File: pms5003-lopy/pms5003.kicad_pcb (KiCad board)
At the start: 2 copper layers, 60 x 56 mm, 24 parts, among them J1 Battery, J2 DS3231, J3 PMS5003, J4 SHT10, J5 P2, J6 PROG, J7 USB_OTG, Q1 IRF540N, Q2 IRF7309IPBF, U1 U3V12F5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

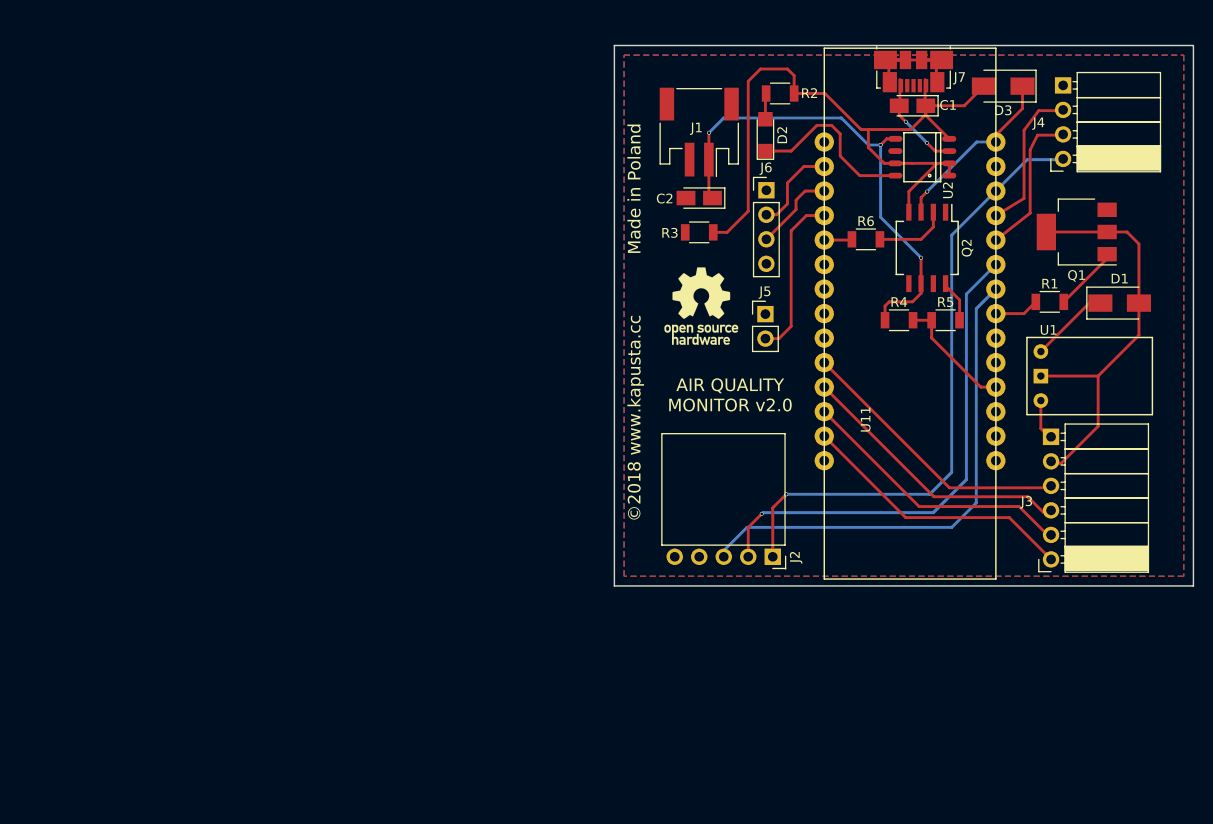
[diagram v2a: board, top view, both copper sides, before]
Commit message: PMS5003-lopy with AQ monitor on the board
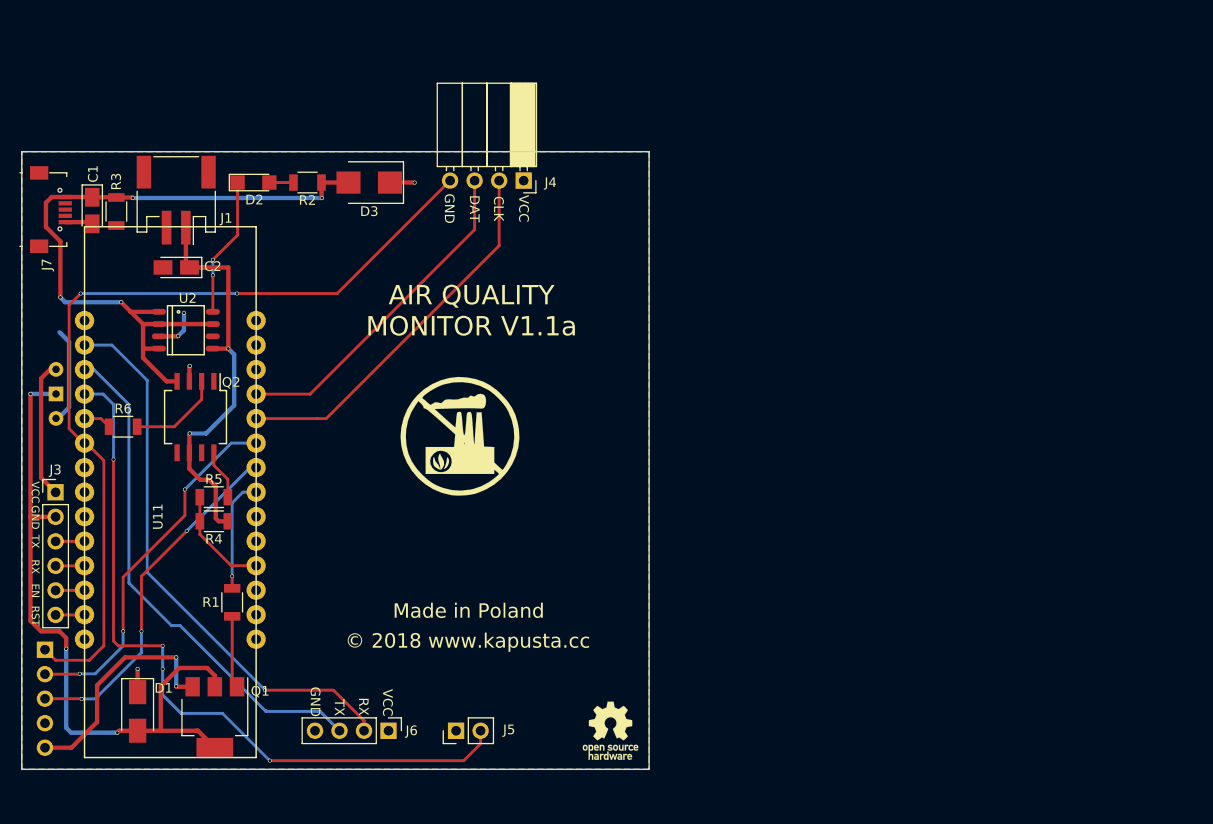
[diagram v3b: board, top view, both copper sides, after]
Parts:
- removed the REF*** at (130.0, 52.0)
- added G***: LOGO, various:pollution, F.Cu at (105.0, 65.5)
- added REF***: OSHW-Logo_5.7x6mm_SilkScreen, Symbols:OSHW-Logo_5.7x6mm_SilkScreen, F.Cu at (120.6, 96.0)
- D3: footprint Diodes_SMD:D_SMA -> Diodes_SMD:D_SMB
- J2, U1: moved to B.Cu
- J3: footprint PMS5003 -> Pin_Headers:Pin_Header_Straight_1x06_Pitch2.54mm
- J4: footprint SHT10 -> Socket_Strips:Socket_Strip_Angled_1x04_Pitch2.54mm
- J7: footprint Connectors_USB:USB_Micro-B_Molex_47346-0001 -> various:USB_Micro-B_91-US01-517
- R2: value 100 -> 470
- moved D1 110.2 mm to (71.6, 94.0), turned to 270 degrees
- moved J3 103.4 mm to (63.1, 71.3), turned to 0 degrees
- moved U1 102.5 mm to (74.7, 65.1)
- moved Q1 102.5 mm to (79.6, 94.6), turned to 270 degrees
- moved J7 90.7 mm to (62.6, 42.0), turned to 270 degrees
- moved R1 90.3 mm to (81.4, 82.7), turned to 270 degrees
- moved C1 85.7 mm to (66.9, 42.1), turned to 270 degrees
- moved R6 79.4 mm to (70.1, 64.5)
- moved U11 78.9 mm to (66.1, 53.5)
- moved U2 78.4 mm to (76.6, 54.5), turned to 270 degrees
- moved R5 78.0 mm to (79.5, 71.8)
- moved Q2 77.8 mm to (77.6, 63.5)
- moved J2 76.0 mm to (62.0, 87.6), turned to 180 degrees
- moved R4 74.0 mm to (79.5, 74.3), turned to 180 degrees
- moved J6 68.3 mm to (97.6, 96.0), turned to 270 degrees
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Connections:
- J2 pad 1: 3V3 -> SHT_RTC_VCC
- J4 pad 4: 3V3 -> SHT_RTC_VCC
- U11 pad 24: SHT10_DATA -> SHT10_SCK
- U11 pad 25: SHT10_SCK -> SHT10_DATA
- U11 pad 26: 3V3 -> (no net)
- U11 pad 6: (no net) -> SHT_RTC_VCC
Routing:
- net SHT_RTC_VCC: track 0.00 -> 89.1 mm, vias 0 -> 2
- net 3V3: track 64.5 -> 0.00 mm, vias 1 -> 0
- net P2: track 17.2 -> 76.2 mm, vias 0 -> 4
- net RX: track 9.34 -> 57.8 mm, vias 0 -> 1
- net TX: track 8.65 -> 53.0 mm
- net 5V_GND: track 43.2 -> 72.1 mm, vias 0 -> 3
- net Net-(J3-Pad6): track 29.0 -> 3.01 mm
- net Net-(J3-Pad4): track 28.9 -> 3.01 mm
- net Net-(J3-Pad5): track 28.9 -> 3.01 mm
- net Net-(J3-Pad3): track 28.9 -> 3.01 mm
- net SHT10_SCK: track 15.3 -> 39.3 mm
- net -USB: track 11.0 -> 32.0 mm, vias 2 -> 4
- net SHT10_DATA: track 15.5 -> 34.8 mm
- net RTC_SCL: track 51.8 -> 36.4 mm, vias 0 -> 3
- net Net-(J7-Pad6): track 14.9 -> 0.00 mm
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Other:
- board size 60 x 56 mm -> 65 x 64 mm
- net class Power added: clearance 0.2, trace_width 0.45, via_dia 0.4, via_drill 0.3
- board text added: "AIR QUALITY MONITOR V1.1a"
- board text added: "CLK"
- board text added: "DAT"
- board text added: "EN"
- board text added: "GND"
- board text added: "Made in Poland"
- board text added: "RST"
- board text added: "RX"
- board text added: "SCL"
- board text added: "SDA"
- board text added: "TX"
- board text added: "VCC"
- board text added: "VIN"
- board text added: "VOUT"
- board text added: "© 2018 www.kapusta.cc"
- board text removed: "AIR QUALITY MONITOR v2.0"
- board text removed: "Prasłowiańska grusza chroni w swych konarach plebejskiego uciekiniera"
- board text removed: "©2018 www.kapusta.cc Made in Poland"

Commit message: Add a pull-up resistor to RTC_VCC
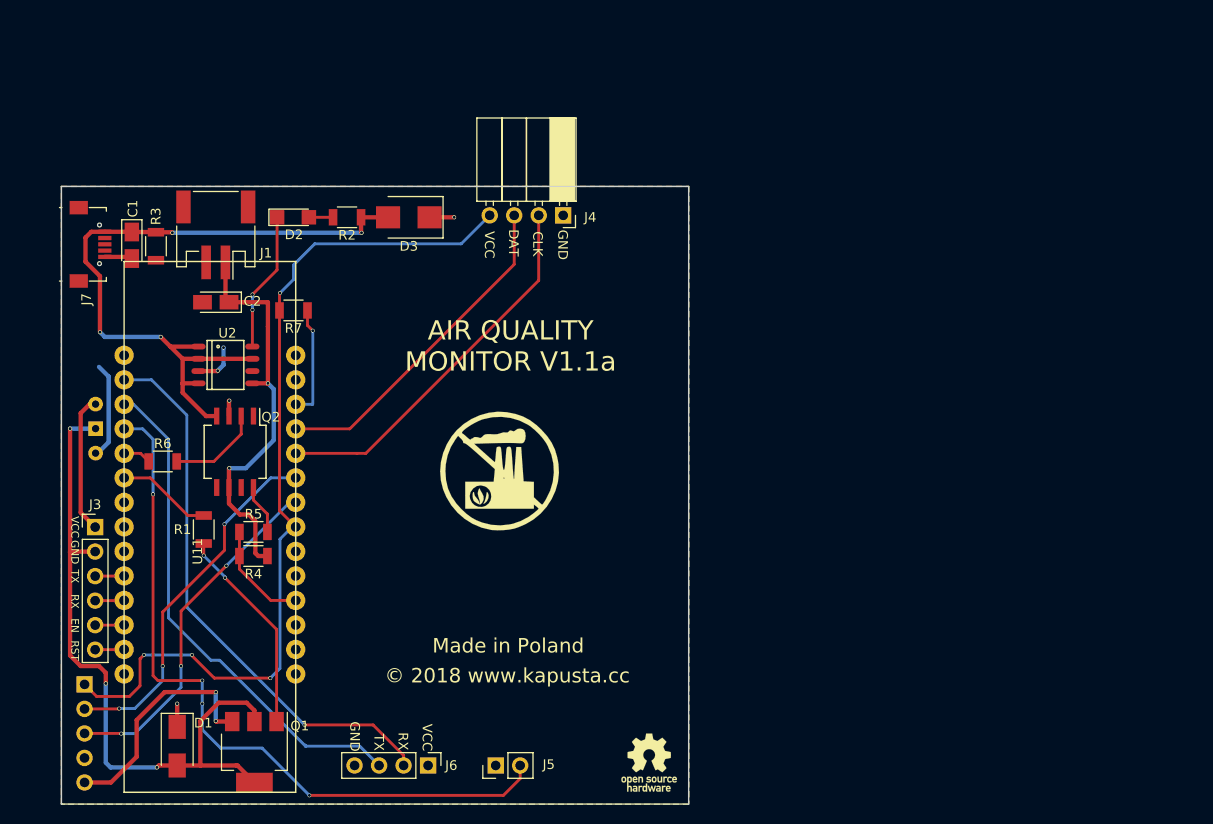
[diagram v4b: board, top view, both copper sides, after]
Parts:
- added R7: 100, Resistors_SMD:R_1206, F.Cu at (87.8, 52.5)
- J3: footprint Pin_Headers:Pin_Header_Straight_1x06_Pitch2.54mm -> Socket_Strips:Socket_Strip_Straight_1x06_Pitch2.54mm
- moved R1 8.11 mm to (78.5, 75.2)
- moved Q1 5.46 mm to (83.7, 98.2)
- moved C2 5.46 mm to (79.7, 51.6)
- moved J1 5.46 mm to (79.7, 44.6)
- moved J4 5.46 mm to (115.7, 42.6)
- moved U11 5.46 mm to (70.2, 57.1)
- moved U2 5.46 mm to (80.7, 58.1)
- moved J3 5.46 mm to (67.2, 74.9)
- moved D1 5.46 mm to (75.7, 97.6)
- moved D2 5.46 mm to (87.7, 42.8)
- moved D3 5.46 mm to (99.7, 42.8)
- moved J5 5.46 mm to (108.7, 99.6)
- moved J6 5.46 mm to (101.7, 99.6)
- moved J7 5.46 mm to (66.7, 45.6)
- moved Q2 5.46 mm to (81.7, 67.1)
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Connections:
- U11 pad 21: PMS_EN -> SHT_RTC_VCC
- U11 pad 26: (no net) -> 3V3
- U11 pad 6: SHT_RTC_VCC -> PMS_EN
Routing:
- net Net-(Q1-Pad1): track 7.51 -> 22.3 mm, vias 0 -> 2
- net 3V3: track 0.00 -> 12.3 mm, vias 0 -> 1
- net SHT_RTC_VCC: track 89.1 -> 92.1 mm, vias 2 -> 4
- net PMS_EN: track 11.8 -> 10.2 mm, vias 1 -> 0

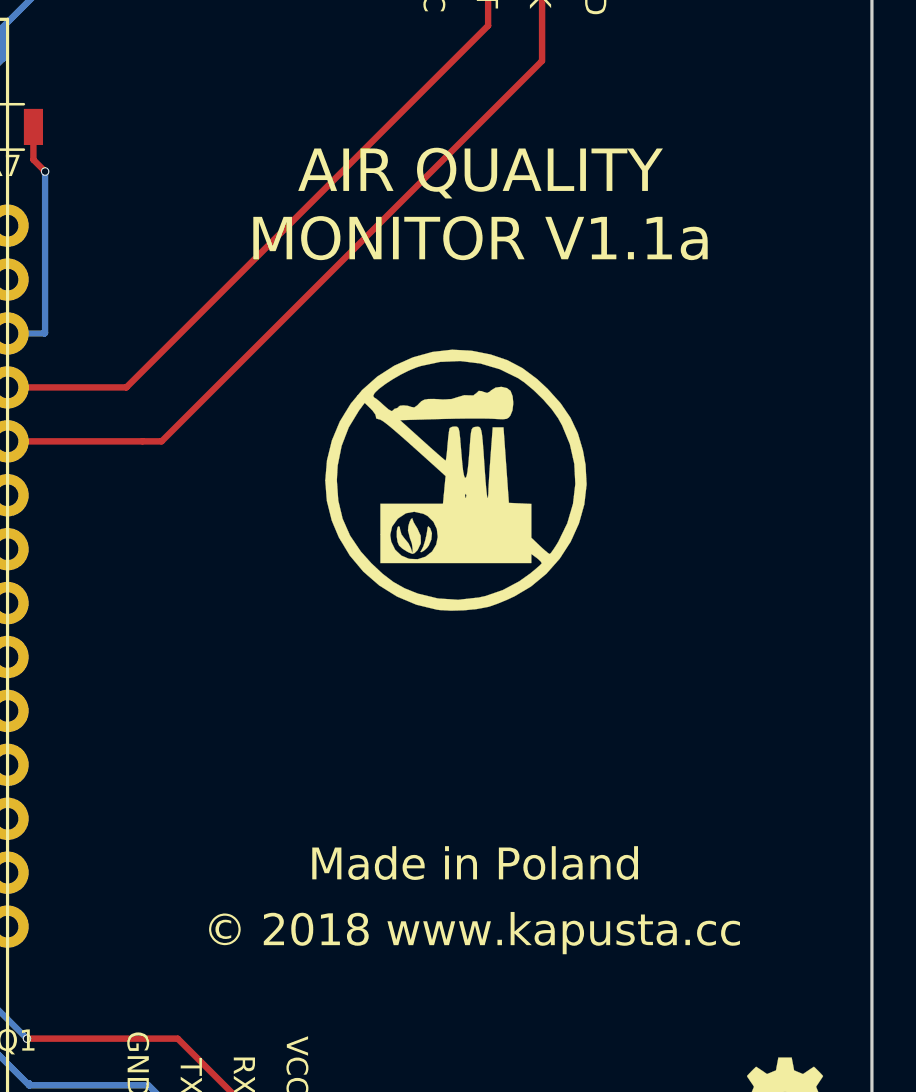
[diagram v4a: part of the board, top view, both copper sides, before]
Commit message: Release PMS5003 in two versions
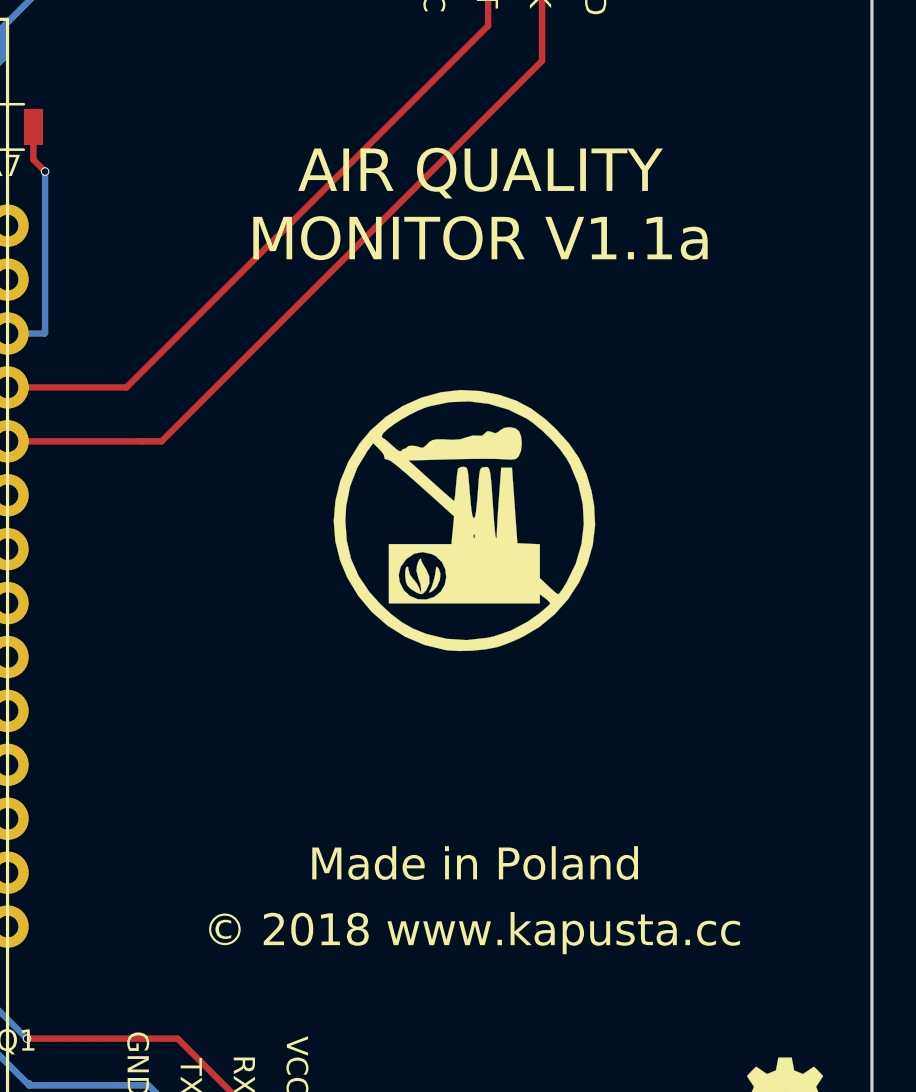
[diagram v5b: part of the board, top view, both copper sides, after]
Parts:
- moved G*** 1.94 mm to (109.5, 71.0)
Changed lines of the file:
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@@
     (area 63.624999 39.524999 128.775001 103.675001)
     (thickness 1.6)
-    (drawings 30)
+    (drawings 34)
     (tracks 268)
     (zones 0)
@@
   )
   (module various:pollution (layer F.Cu)
-    (at 109.1 69.1)
+    (at 109.5 71)
     (fp_text reference G*** (at 0 0) (layer F.SilkS) hide
       (effects (font (thickness 0.3)))
@@
     )
   )
+  (dimension 25.5 (width 0.3) (layer Cmts.User)
+    (gr_text "25.500 mm" (at 103.65 58.75 270) (layer Cmts.User)
+      (effects (font (size 1.5 1.5) (thickness 0.3)))
+    )
+    (feature1 (pts (xy 129 71.5) (xy 102.3 71.5)))
+    (feature2 (pts (xy 129 46) (xy 102.3 46)))
+    (crossbar (pts (xy 105 46) (xy 105 71.5)))
+    (arrow1a (pts (xy 105 71.5) (xy 104.413579 70.373496)))
+    (arrow1b (pts (xy 105 71.5) (xy 105.586421 70.373496)))
+    (arrow2a (pts (xy 105 46) (xy 104.413579 47.126504)))
+    (arrow2b (pts (xy 105 46) (xy 105.586421 47.126504)))
+  )
+  (dimension 19.25 (width 0.3) (layer Cmts.User)
+    (gr_text "19.250 mm" (at 99.875 74.85) (layer Cmts.User)
+      (effects (font (size 1.5 1.5) (thickness 0.3)))
+    )
+    (feature1 (pts (xy 109.5 46) (xy 109.5 76.2)))
+    (feature2 (pts (xy 90.25 46) (xy 90.25 76.2)))
+    (crossbar (pts (xy 90.25 73.5) (xy 109.5 73.5)))
+    (arrow1a (pts (xy 109.5 73.5) (xy 108.373496 74.086421)))
+    (arrow1b (pts (xy 109.5 73.5) (xy 108.373496 72.913579)))
+    (arrow2a (pts (xy 90.25 73.5) (xy 91.376504 74.086421)))
+    (arrow2b (pts (xy 90.25 73.5) (xy 91.376504 72.913579)))
+  )
+  (dimension 38.5 (width 0.3) (layer Cmts.User)
+    (gr_text "38.500 mm" (at 109.45 29.65) (layer Cmts.User)
+      (effects (font (size 1.5 1.5) (thickness 0.3)))
+    )
+    (feature1 (pts (xy 90.2 46.1) (xy 90.2 28.3)))
+    (feature2 (pts (xy 128.7 46.1) (xy 128.7 28.3)))
+    (crossbar (pts (xy 128.7 31) (xy 90.2 31)))
+    (arrow1a (pts (xy 90.2 31) (xy 91.326504 30.413579)))
+    (arrow1b (pts (xy 90.2 31) (xy 91.326504 31.586421)))
+    (arrow2a (pts (xy 128.7 31) (xy 127.573496 30.413579)))
+    (arrow2b (pts (xy 128.7 31) (xy 127.573496 31.586421)))
+  )
+  (dimension 51 (width 0.3) (layer Cmts.User)
+    (gr_text "51.000 mm" (at 134.55 71.6 90) (layer Cmts.User)
+      (effects (font (size 1.5 1.5) (thickness 0.3)))
+    )
+    (feature1 (pts (xy 128.7 46.1) (xy 135.9 46.1)))
+    (feature2 (pts (xy 128.7 97.1) (xy 135.9 97.1)))
+    (crossbar (pts (xy 133.2 97.1) (xy 133.2 46.1)))
+    (arrow1a (pts (xy 133.2 46.1) (xy 133.786421 47.226504)))
+    (arrow1b (pts (xy 133.2 46.1) (xy 132.613579 47.226504)))
+    (arrow2a (pts (xy 133.2 97.1) (xy 133.786421 95.973496)))
+    (arrow2b (pts (xy 133.2 97.1) (xy 132.613579 95.973496)))
+  )
   (gr_text VCC (at 108.05 45.65 270) (layer F.SilkS)
     (effects (font (size 1 1) (thickness 0.2)))
   )
-  (gr_text "Made in Poland" (at 110 87.2 360) (layer F.SilkS)
+  (gr_text "Made in Poland" (at 110 87.2) (layer F.SilkS)
     (effects (font (size 1.5 1.5) (thickness 0.3)))
   )
-  (gr_text "© 2018 www.kapusta.cc" (at 109.9 90.3 360) (layer F.SilkS)
+  (gr_text "© 2018 www.kapusta.cc" (at 109.9 90.3) (layer F.SilkS)
     (effects (font (size 1.5 1.5) (thickness 0.3)))
   )
-  (gr_text "AIR QUALITY \nMONITOR V1.1a" (at 110.25 56.15 360) (layer F.SilkS)
+  (gr_text "AIR QUALITY \nMONITOR V1.1a" (at 110.25 56.15) (layer F.SilkS)
     (effects (font (size 2 2) (thickness 0.4)))
   )
@@
     (effects (font (size 0.8 0.8) (thickness 0.15)) (justify mirror))
   )
-  (gr_text GND (at 69 101.4 360) (layer B.SilkS)
+  (gr_text GND (at 69 101.4) (layer B.SilkS)
     (effects (font (size 1 1) (thickness 0.2)) (justify mirror))
   )
-  (gr_text SCL (at 69 96.3 360) (layer B.SilkS)
+  (gr_text SCL (at 69 96.3) (layer B.SilkS)
     (effects (font (size 1 1) (thickness 0.2)) (justify mirror))
   )
-  (gr_text SDA (at 69 93.8 360) (layer B.SilkS)
+  (gr_text SDA (at 69 93.8) (layer B.SilkS)
     (effects (font (size 1 1) (thickness 0.2)) (justify mirror))
   )
-  (gr_text VCC (at 69 91.3 360) (layer B.SilkS)
+  (gr_text VCC (at 69 91.3) (layer B.SilkS)
     (effects (font (size 1 1) (thickness 0.2)) (justify mirror))
   )
